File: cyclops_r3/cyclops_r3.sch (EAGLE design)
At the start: 105 parts, among them Q1 BC817, Q2 IRF510, U1 MCP4921, U2 MCP4022-50k, U3 317-N, U4 TLV3701, U5 337-N, U6 ADR03, U7 OP1177, U8 LTC2052HV, U9 ZXTD45

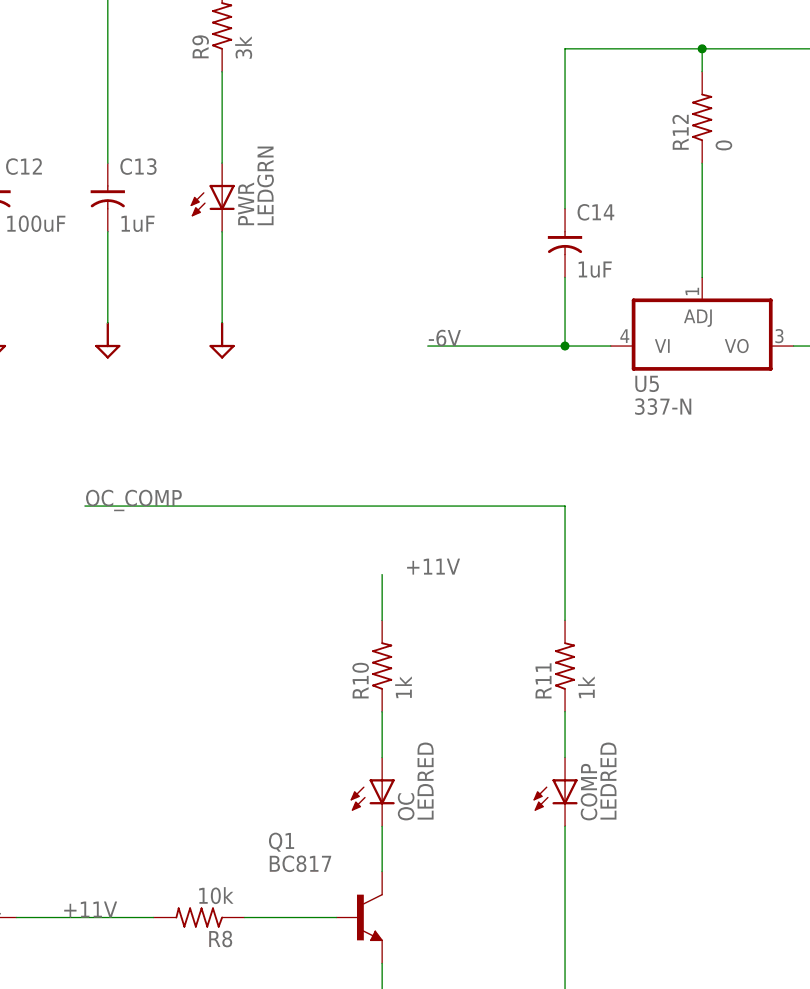
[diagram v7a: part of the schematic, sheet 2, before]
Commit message: Front panel dimensions have been tested and look good. Started integrating light pipes on front panel LEDs. The LEDs need to be moved and swapped for normal verical ones.
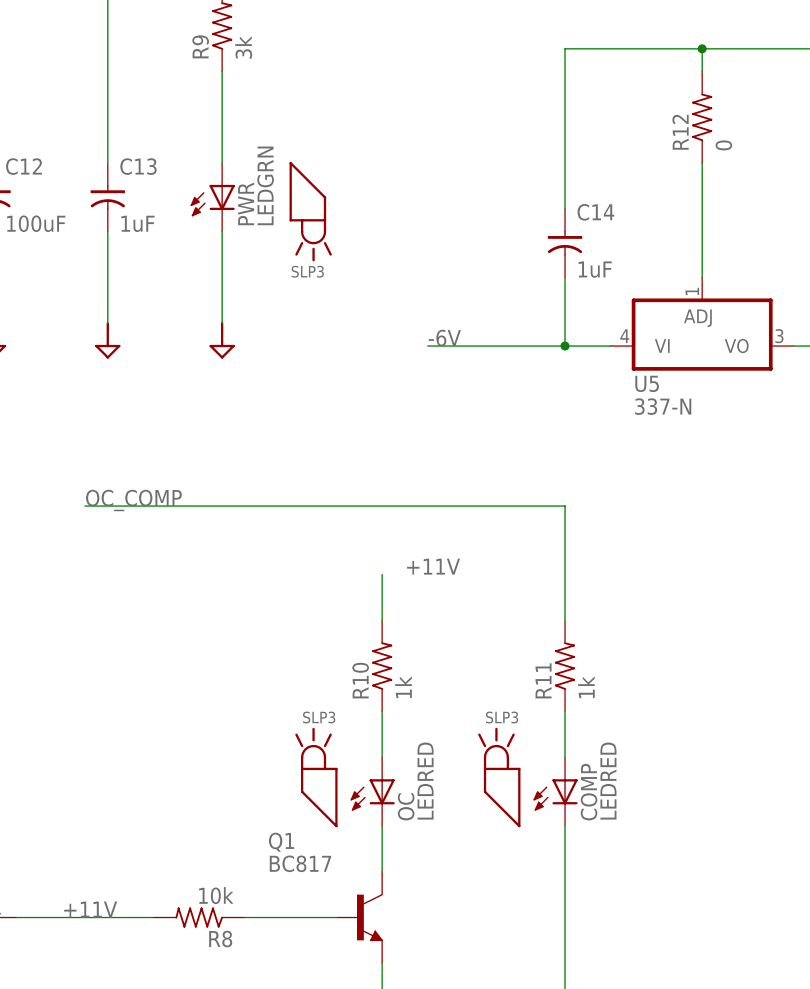
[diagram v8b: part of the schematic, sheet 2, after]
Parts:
- added U$51, U$52, U$53: SLP3, cyclops:LIGHT-PIPE_SL30-150-100-F
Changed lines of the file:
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@@
 <?xml version="1.0" encoding="utf-8"?>
 <!DOCTYPE eagle SYSTEM "eagle.dtd">
-<eagle version="6.6.0">
+<eagle version="6.5.0">
 <drawing>
 <settings>
@@
 <part name="R27" library="cyclops" deviceset="R" device="_0603" value="10k"/>
 <part name="P+7" library="cyclops" deviceset="+5V" device="" value="+5V"/>
+<part name="U$51" library="cyclops" deviceset="LIGHT-PIPE" device="_SL30-150-100-F" value="SLP3"/>
+<part name="U$52" library="cyclops" deviceset="LIGHT-PIPE" device="_SL30-150-100-F" value="SLP3"/>
+<part name="U$53" library="cyclops" deviceset="LIGHT-PIPE" device="_SL30-150-100-F" value="SLP3"/>
 </parts>
 <sheets>
@@
 <instance part="COMP" gate="G$1" x="93.98" y="-68.58"/>
 <instance part="U$49" gate="G$1" x="93.98" y="-114.3"/>
+<instance part="U$51" gate="G$1" x="68.58" y="-73.66" rot="R90"/>
+<instance part="U$52" gate="G$1" x="88.9" y="-73.66" rot="R90"/>
+<instance part="U$53" gate="G$1" x="63.5" y="0" rot="R270"/>
 </instances>
 <busses>
